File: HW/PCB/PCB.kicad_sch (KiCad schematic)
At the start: 54 parts, among them J1 USB4105-GF-A, J4 Micro_SD_Card_Det_Hirose_DM3AT, Q1 2PC4081R, Q2 2PC4081R, SW1 ssss213202, SW2 SKRPACE010, SW3 SKRPACE010, U1 BME280, U2 FT231XS, U3 LT1963ES8-3.3, U4 ESP32-S3-WROOM-1, U5 SCD40, U6 AQM0802A-RN-GBW, U7 TPS2065DDBVR, Y1 FC-135

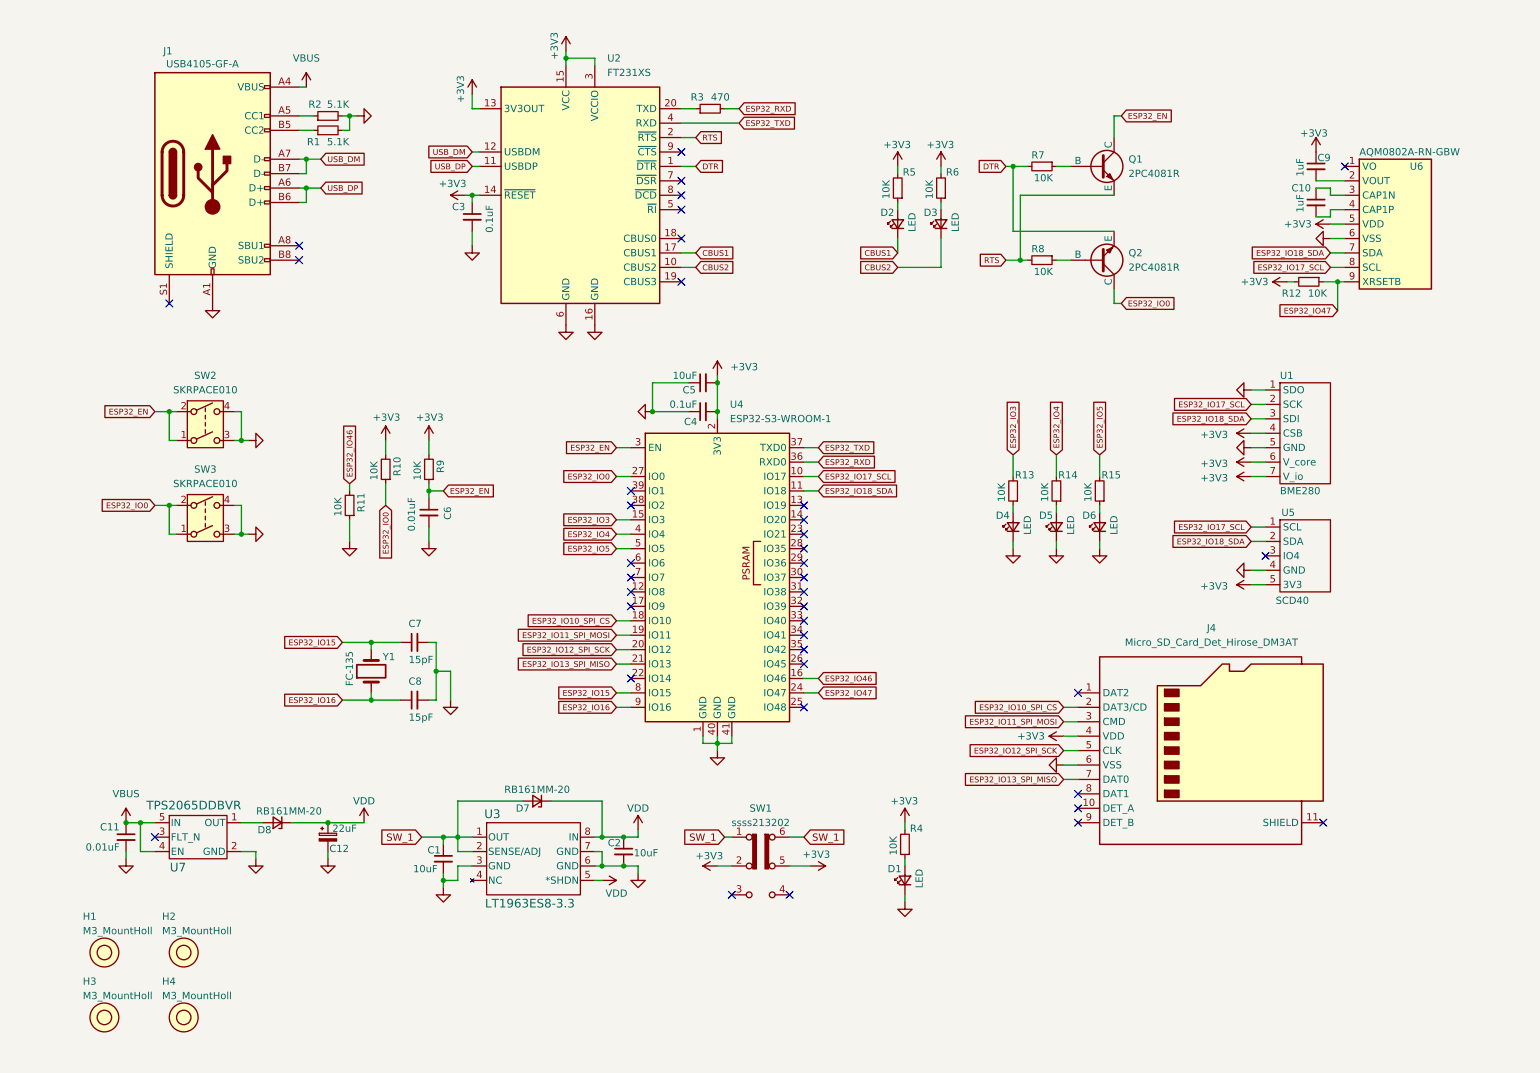
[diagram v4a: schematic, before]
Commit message: add e-paper module
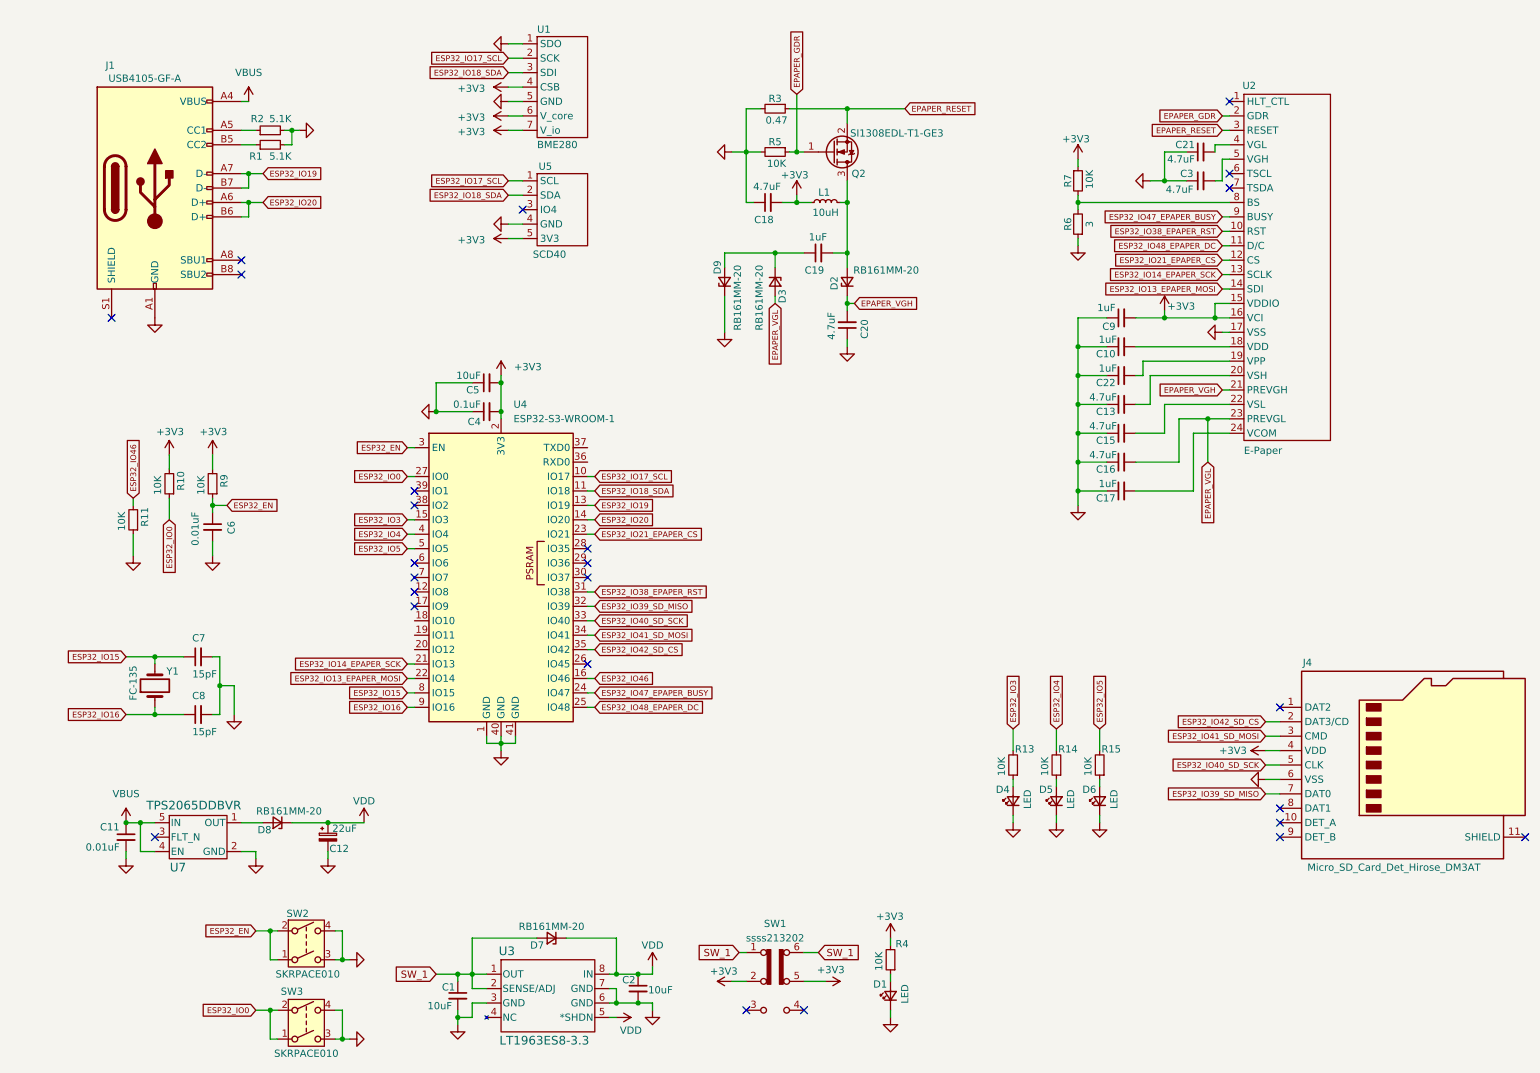
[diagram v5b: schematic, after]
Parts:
- removed D2, D3: LED, LED_SMD:LED_0603_1608Metric_Pad1.05x0.95mm_HandSolder, symbol Device:LED_Small
- removed H1, H2, H3, H4: M3_MountHoll, MountingHole:MountingHole_3.2mm_M3, symbol Mylib:MountHole_M3
- removed Q1, Q2: 2PC4081R, Package_TO_SOT_SMD:SOT-323_SC-70_Handsoldering, symbol Simulation_SPICE:NPN
- removed R12, R8: 10K, Resistor_SMD:R_1206_3216Metric_Pad1.30x1.75mm_HandSolder, symbol Device:R_Small
- removed U2: FT231XS, Package_SO:SSOP-20_3.9x8.7mm_P0.635mm, symbol Interface_USB:FT231XS
- removed U6: AQM0802A-RN-GBW, mylib:AQM0802A-RN-GBW, symbol Mylib:AQM0802A-RN-GBW
- added C13, C15, C16, C18, C20, C21: 4.7uF, Capacitor_SMD:C_0603_1608Metric_Pad1.08x0.95mm_HandSolder, symbol Device:C_Small
- added C17, C19, C22: 1uF, Capacitor_SMD:C_0603_1608Metric_Pad1.08x0.95mm_HandSolder, symbol Device:C_Small
- added D2, D3, D9: RB161MM-20, Diode_SMD:D_SOD-123, symbol Device:D_Zener_Small
- added L1: 10uH, mylib:AMP10420ED, symbol Device:L_Small
- added Q2: SI1308EDL-T1-GE3, Package_TO_SOT_SMD:SOT-323_SC-70_Handsoldering, symbol Transistor_FET:BSS138
- added U2: E-Paper, XF2M-2415-1A:CONN_XF2M-2415-1A_OMR, symbol Mylib:4_26inch_EPaper
- C3: value 0.1uF -> 4.7uF; footprint Capacitor_SMD:C_0805_2012Metric_Pad1.18x1.45mm_HandSolder -> Capacitor_SMD:C_0603_1608Metric_Pad1.08x0.95mm_HandSolder
- J1: footprint Connector_USB:USB_C_Receptacle_GCT_USB4105-xx-A_16P_TopMnt_Horizontal -> mylib:USB-C31-S-VT-CS4-BK-PP-TR
- R3: value 470 -> 0.47
- R6: value 10K -> 3
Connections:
- net USB_DM is gone; now on net ESP32_IO19: J1.A7 (D-), J1.B7 (D-)
- net USB_DP is gone; now on net ESP32_IO20: J1.A6 (D+), J1.B6 (D+)
- net +3V3: now also C9.2, R7.1, C18.2, L1.1, U2.15 (VDDIO), U2.16 (VCI); no longer C3.1, C9.1, R5.2, R6.2
- net GND: now also C10.1, C3.1, C9.1, R3.2, R5.2, R6.1, C13.1, C15.1, C16.1, C17.1, C18.1, C20.1, C21.1, C22.1, D9.1 (K), U2.17 (VSS); no longer C3.2
- net EPAPER_RESET: now reaches R3.1
- net EPAPER_RESET: now also Q2.2 (S), U2.3 (RESET)
- net ESP32_IO19: now reaches U4.13 (IO19)
- net ESP32_IO20: now reaches U4.14 (IO20)
- net ESP32_IO13_EPAPER_MOSI: now reaches U4.22 (IO14)
- net ESP32_IO13_EPAPER_MOSI: now also U2.14 (SDI)
- net ESP32_IO21_EPAPER_CS: now reaches U4.23 (IO21)
- net ESP32_IO21_EPAPER_CS: now also U2.12 (CS)
- net ESP32_IO48_EPAPER_DC: now reaches U4.25 (IO48)
- net ESP32_IO48_EPAPER_DC: now also U2.11 (D/C)
- net ESP32_IO38_EPAPER_RST: now reaches U4.31 (IO38)
- net ESP32_IO38_EPAPER_RST: now also U2.10 (RST)
- net ESP32_IO39_SD_MISO: now reaches U4.32 (IO39)
- net ESP32_IO39_SD_MISO: now also J4.7 (DAT0)
- net ESP32_IO40_SD_SCK: now reaches U4.33 (IO40)
- net ESP32_IO40_SD_SCK: now also J4.5 (CLK)
- net ESP32_IO41_SD_MOSI: now reaches U4.34 (IO41)
- net ESP32_IO41_SD_MOSI: now also J4.3 (CMD)
- net ESP32_IO42_SD_CS: now reaches U4.35 (IO42)
- net ESP32_IO42_SD_CS: now also J4.2 (DAT3/CD)
- net EPAPER_GDR: now reaches R5.1
- net EPAPER_GDR: now also Q2.1 (G), U2.2 (GDR)
- net at C10.2: now also U2.18 (VDD)
- net DTR: no longer names the net of R7.2
- net DTR: now also R6.2, U2.8 (BS)
- net ESP32_IO10_SPI_CS: no longer names the net of U4.18 (IO10)
- net ESP32_IO10_SPI_CS: no longer J4.2 (DAT3/CD)
- net ESP32_IO11_SPI_MOSI: no longer names the net of U4.19 (IO11)
- net ESP32_IO11_SPI_MOSI: no longer J4.3 (CMD)
- net ESP32_IO12_SPI_SCK: no longer names the net of U4.20 (IO12)
- net ESP32_IO12_SPI_SCK: no longer J4.5 (CLK)
- net ESP32_IO13_SPI_MISO renamed ESP32_IO14_EPAPER_SCK
- net ESP32_IO14_EPAPER_SCK: now also U2.13 (SCLK); no longer J4.7 (DAT0)
- net ESP32_IO47 renamed ESP32_IO47_EPAPER_BUSY
- net ESP32_IO47_EPAPER_BUSY: now also U2.9 (BUSY)
- net ESP32_RXD: no longer names the net of U4.36 (RXD0)
- net ESP32_RXD: no longer R3.2
- net ESP32_TXD: no longer names the net of U4.37 (TXD0)
- new net: C3.2, U2.5 (VGH)
- new net: C22.2, U2.19 (VPP)
- new net: C13.2, U2.20 (VSH)
- new net: C15.2, U2.22 (VSL)
- new net: C17.2, U2.24 (VCOM)
- new net: C21.2, U2.4 (VGL)
- new net: C19.2, D2.2 (A), L1.2, Q2.3 (D)
- new net: C19.1, D3.1 (K), D9.2 (A)
- new net EPAPER_VGH: C20.2, D2.1 (K), U2.21 (PREVGH)
- new net EPAPER_VGL: C16.2, D3.2 (A), U2.23 (PREVGL)
- no-connect marks 39 -> 25
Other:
- moved on the sheet: C1, C2, C4, C5, C6, C7, C8, D1, D4, D5, D6, D7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

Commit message: modify schematics
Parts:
- removed U3: LT1963ES8-3.3, Package_SO:Infineon_PG-DSO-8-24_4x5mm, symbol 2024-10-06_05-34-51:LT1963ES8-1.8-PBF
- added U6: AZ1117CH-3_3TRG1, Package_TO_SOT_SMD:SOT-223, symbol dk_PMIC-Voltage-Regulators-Linear:AZ1117CH-3_3TRG1
- C2: value 10uF -> 22uF
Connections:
- net GND: now also U6.1 (ADJ/GND)
- net SW_1: now also C2.1, U6.2 (OUT), U6.4 (VOUT); no longer C1.1
- net VDD: now also C1.1, U6.3 (IN); no longer C2.1
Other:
- moved on the sheet: C1, C10, C13, C15, C16, C17, C2, C21, C22, C3, C9, D7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

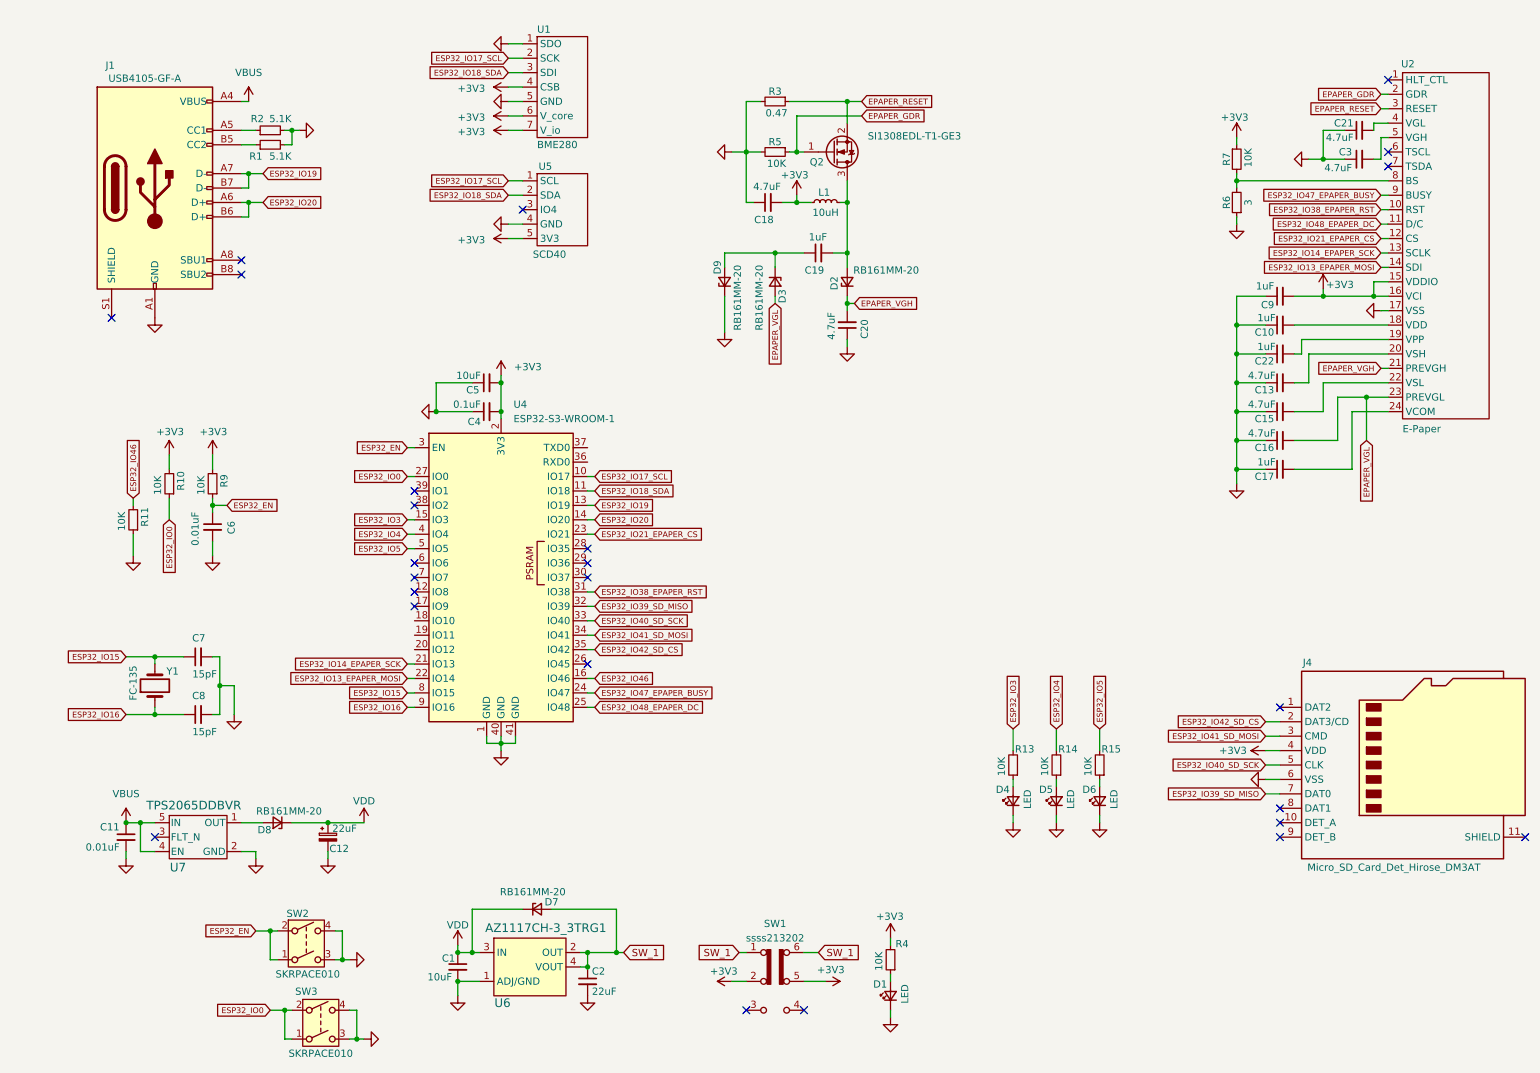
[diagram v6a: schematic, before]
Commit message: modify PCB layout
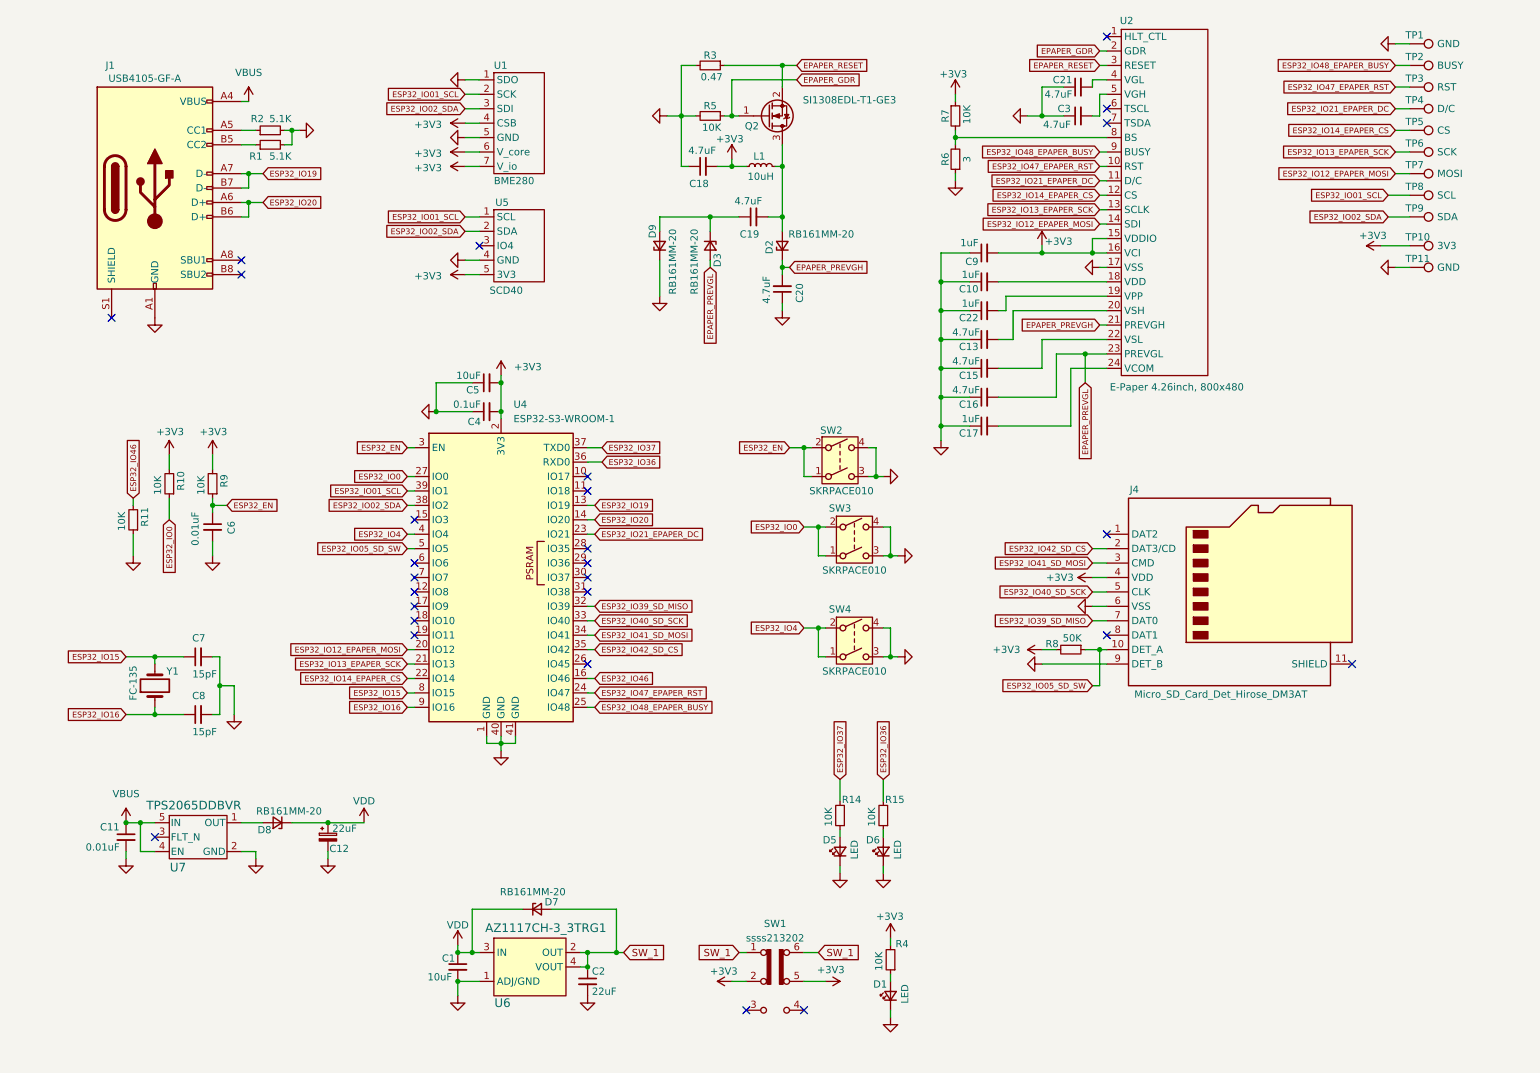
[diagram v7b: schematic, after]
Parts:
- removed D4: LED, LED_SMD:LED_0603_1608Metric_Pad1.05x0.95mm_HandSolder, symbol Device:LED_Small
- removed R13: 10K, Resistor_SMD:R_1206_3216Metric_Pad1.30x1.75mm_HandSolder, symbol Device:R_Small
- added R8: 50K, Resistor_SMD:R_1206_3216Metric_Pad1.30x1.75mm_HandSolder, symbol Device:R_Small
- added SW4: SKRPACE010, mylib:SKRPACE010, symbol Switch:SW_DPST
- added TP1, TP11: GND, TestPoint:TestPoint_THTPad_1.0x1.0mm_Drill0.5mm, symbol Connector:TestPoint
- added TP10: 3V3, TestPoint:TestPoint_THTPad_D1.0mm_Drill0.5mm, symbol Connector:TestPoint
- added TP2: BUSY, TestPoint:TestPoint_THTPad_D1.0mm_Drill0.5mm, symbol Connector:TestPoint
- added TP3: RST, TestPoint:TestPoint_THTPad_D1.0mm_Drill0.5mm, symbol Connector:TestPoint
- added TP4: D/C, TestPoint:TestPoint_THTPad_D1.0mm_Drill0.5mm, symbol Connector:TestPoint
- added TP5: CS, TestPoint:TestPoint_THTPad_D1.0mm_Drill0.5mm, symbol Connector:TestPoint
- added TP6: SCK, TestPoint:TestPoint_THTPad_D1.0mm_Drill0.5mm, symbol Connector:TestPoint
- added TP7: MOSI, TestPoint:TestPoint_THTPad_D1.0mm_Drill0.5mm, symbol Connector:TestPoint
- added TP8: SCL, TestPoint:TestPoint_THTPad_D1.0mm_Drill0.5mm, symbol Connector:TestPoint
- added TP9: SDA, TestPoint:TestPoint_THTPad_D1.0mm_Drill0.5mm, symbol Connector:TestPoint
- C19: value 1uF -> 4.7uF
- U2: value E-Paper -> E-Paper 4.26inch, 800x480
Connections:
- net +3V3: now also R8.2, TP10.1
- net ESP32_IO4: now also SW4.1, SW4.2; no longer R14.2
- net GND: now also J4.9 (DET_B), SW4.3, SW4.4, TP1.1, TP11.1
- net ESP32_IO12_EPAPER_MOSI: now reaches U4.20 (IO12)
- net ESP32_IO12_EPAPER_MOSI: now also U2.14 (SDI), TP7.1
- net ESP32_IO36: now reaches U4.36 (RXD0)
- net ESP32_IO36: now also R15.2
- net ESP32_IO37: now reaches U4.37 (TXD0)
- net ESP32_IO37: now also R14.2
- net ESP32_IO02_SDA: now reaches U4.38 (IO2)
- net ESP32_IO02_SDA: now also U1.3 (SDI), U5.2 (SDA), TP9.1
- net ESP32_IO01_SCL: now reaches U4.39 (IO1)
- net ESP32_IO01_SCL: now also U1.2 (SCK), U5.1 (SCL), TP8.1
- net ESP32_IO05_SD_SW: now reaches J4.10 (DET_A)
- net ESP32_IO05_SD_SW: now also U4.5 (IO5), R8.1
- net EPAPER_VGH renamed EPAPER_PREVGH
- net EPAPER_VGL renamed EPAPER_PREVGL
- net ESP32_IO13_EPAPER_MOSI renamed ESP32_IO14_EPAPER_CS
- net ESP32_IO14_EPAPER_CS: now also U2.12 (CS), TP5.1; no longer U2.14 (SDI)
- net ESP32_IO14_EPAPER_SCK renamed ESP32_IO13_EPAPER_SCK
- net ESP32_IO13_EPAPER_SCK: now also TP6.1
- removed net ESP32_IO17_SCL: U1.2 (SCK), U4.10 (IO17), U5.1 (SCL)
- removed net ESP32_IO18_SDA: U1.3 (SDI), U4.11 (IO18), U5.2 (SDA)
- net ESP32_IO21_EPAPER_CS renamed ESP32_IO21_EPAPER_DC
- net ESP32_IO21_EPAPER_DC: now also U2.11 (D/C), TP4.1; no longer U2.12 (CS)
- net ESP32_IO3: no longer names the net of U4.15 (IO3)
- net ESP32_IO38_EPAPER_RST: no longer names the net of U4.31 (IO38)
- net ESP32_IO38_EPAPER_RST: no longer U2.10 (RST)
- net ESP32_IO47_EPAPER_BUSY renamed ESP32_IO47_EPAPER_RST
- net ESP32_IO47_EPAPER_RST: now also U2.10 (RST), TP3.1; no longer U2.9 (BUSY)
- net ESP32_IO48_EPAPER_DC renamed ESP32_IO48_EPAPER_BUSY
- net ESP32_IO48_EPAPER_BUSY: now also U2.9 (BUSY), TP2.1; no longer U2.11 (D/C)
- removed net ESP32_IO5: R15.2, U4.5 (IO5)
- no-connect marks 25 -> 27
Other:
- moved on the sheet: C10, C13, C15, C16, C17, C18, C19, C20, C21, C22, C3, C9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
